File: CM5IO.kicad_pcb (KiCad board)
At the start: 4 copper layers, 160 x 90 mm, 76 parts, among them J10 690-019-298-412, J11 USB_C_Receptacle_USB2.0, J12 USB3_A, J14 JST_SHBM04B-SRSS-TB, J16 Conn_01x22_Female, J2 Conn_02x07_Odd_Even, J22 690-019-298-412, J3 Conn_01x03, J4 Bus_M.2_Socket_M, J5 Conn_01x22_Female, J6 THD-02-R, J7 Micro_SD_Card_Det, J8 THD-20-R, J9 THD-02-R, SW1 Right angle Tact button, U1 TPD4EUSB30, U12 RT9742SNGV, U18 RT9742GGJ5, U2 TPD4EUSB30, U3 MagJack-A70-112-331N126, U5 74LVC1G07SE-7, U6 AP22653W6, U7 ASEK-32.768KHZ-L-R-T, U8 AP3441SHE-7B

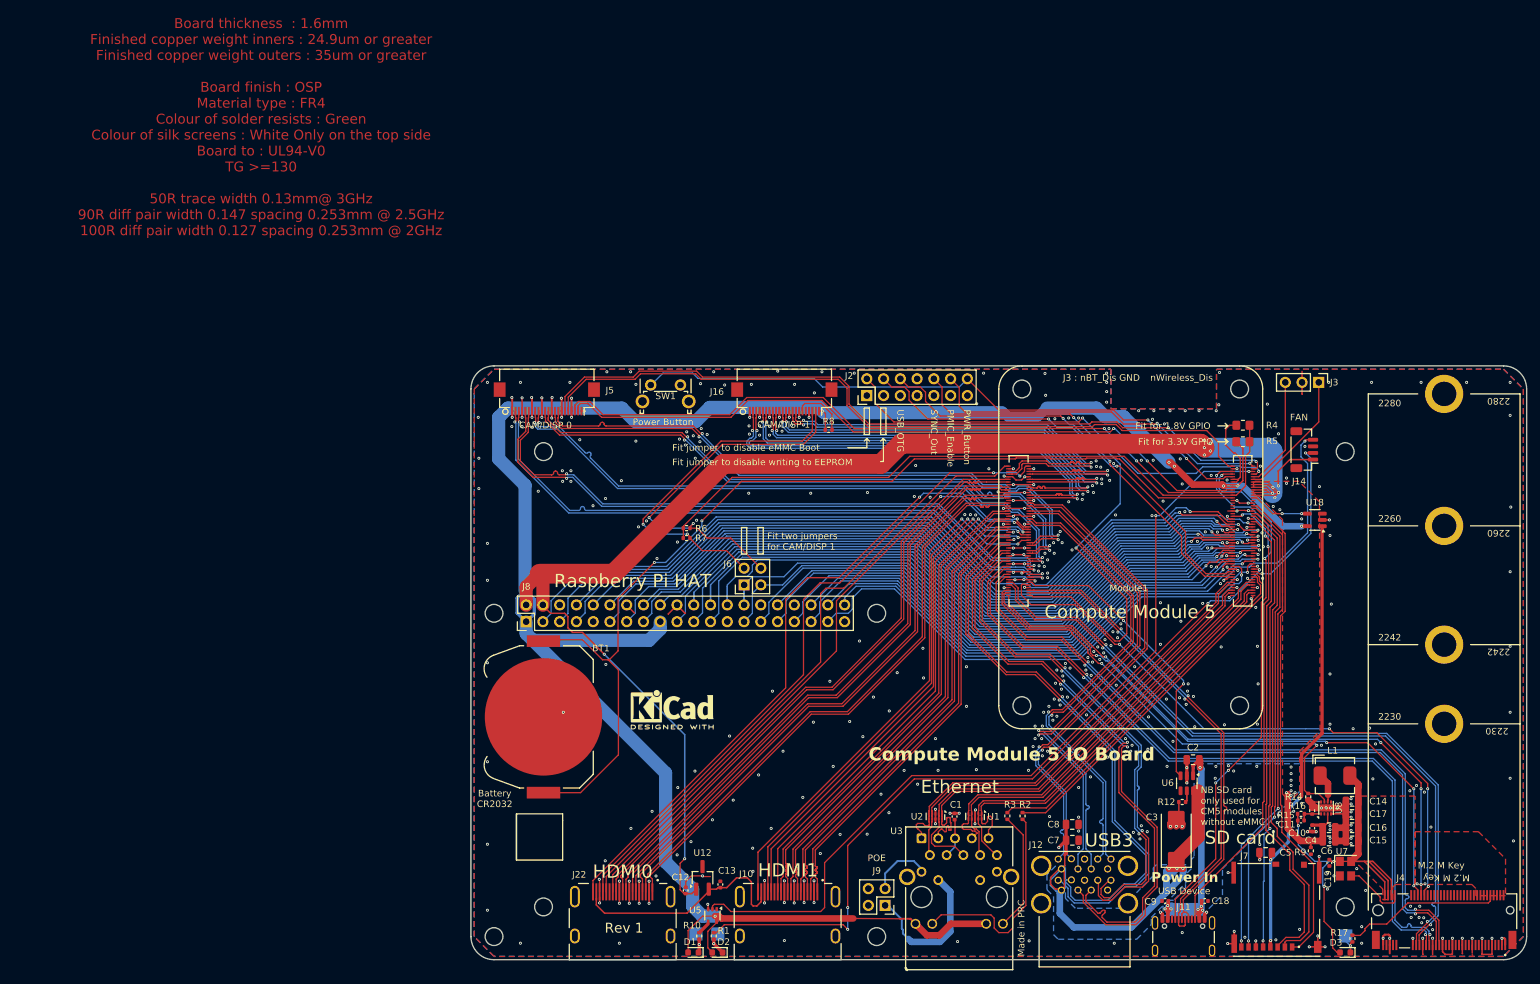
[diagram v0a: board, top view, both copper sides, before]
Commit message: remove ethernet, pcie, hdmi
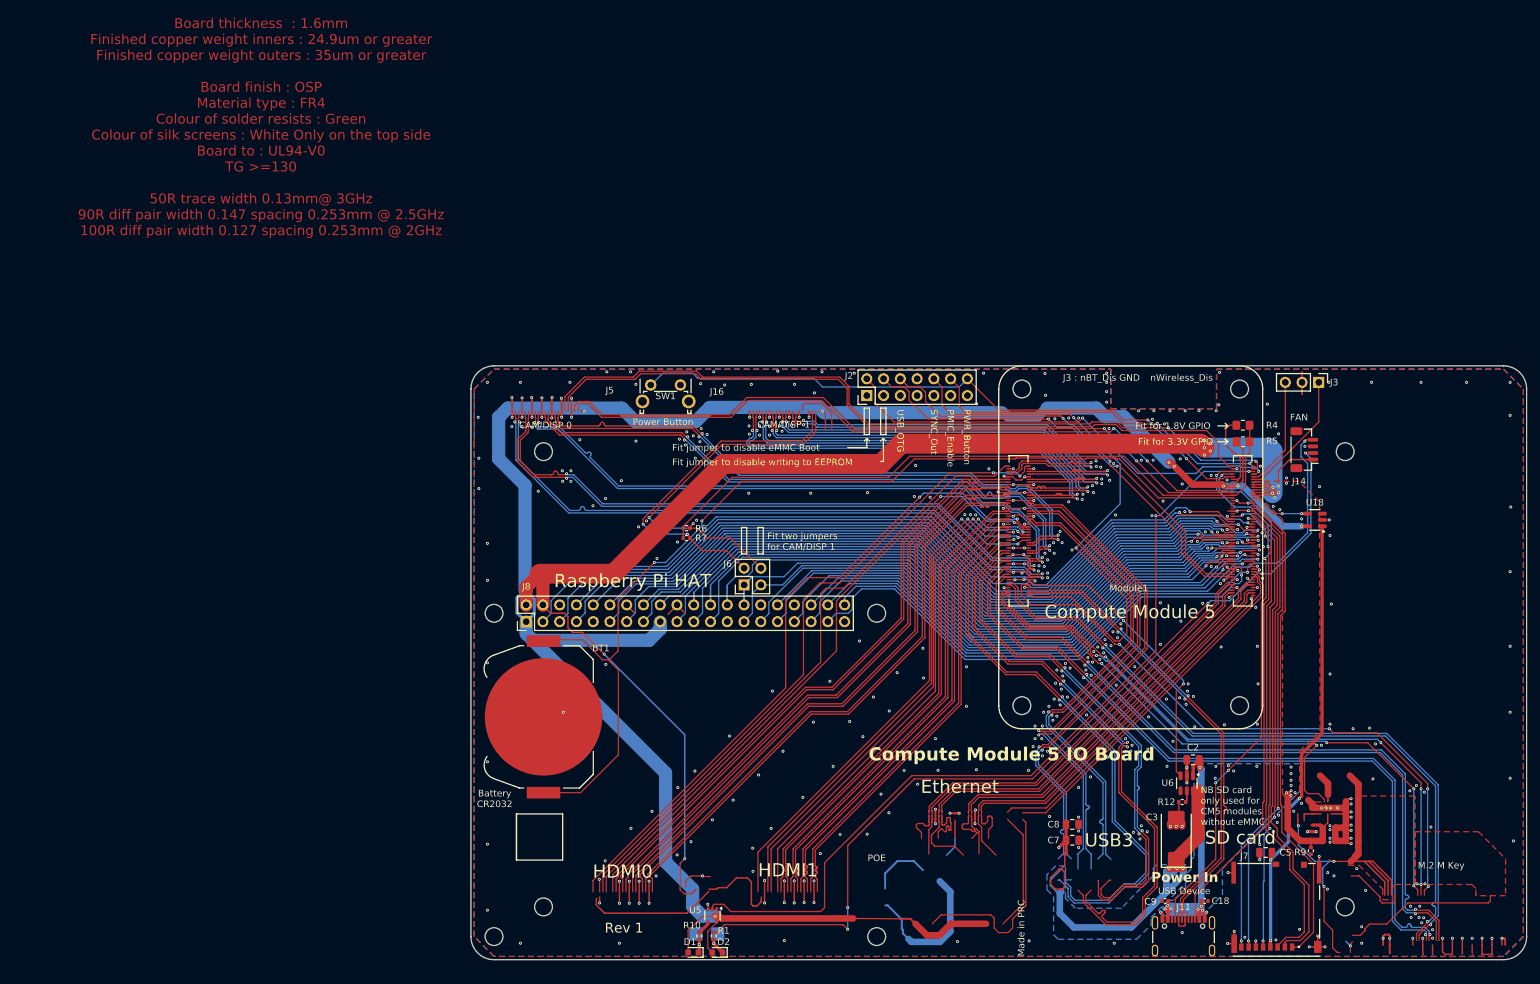
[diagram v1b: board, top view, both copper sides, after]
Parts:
- removed C1, C10, C12, C13, C19: 100n, Capacitor_SMD:C_0402_1005Metric
- removed C11: 4.7nF, Capacitor_SMD:C_0402_1005Metric
- removed C14, C15, C16, C17, C4, C6: 10u, Capacitor_SMD:C_0805_2012Metric
- removed D3: LED Green, LED_SMD:LED_0603_1608Metric
- removed J10, J22: 690-019-298-412, CM5IO:EDAC 690-019-298-412
- removed J12: USB3_A, CM5IO:MTCONN_UBAF30-D2011
- removed J16, J5: Conn_01x22_Female, CM5IO:Hirose_FH12-22S-0.5SH_1x22-1MP_P0.50mm_Horizontal
- removed J4: Bus_M.2_Socket_M, CM5IO:M.2 M Key socket
- removed J9: THD-02-R, Connector_PinHeader_2.54mm:PinHeader_2x02_P2.54mm_Vertical
- removed L1: 2.2uH, CM5IO:L_Bourns_SRP5030CC
- removed R14: 100K 1%, Resistor_SMD:R_0402_1005Metric
- removed R15: 10K 1%, Resistor_SMD:R_0402_1005Metric
- removed R16, R8: 2.2K 1%, Resistor_SMD:R_0402_1005Metric
- removed R17: 1k, Resistor_SMD:R_0402_1005Metric
- removed R2, R3: 470R, Resistor_SMD:R_0402_1005Metric
- removed TP1: TestPoint, TestPoint:TestPoint_Pad_2.0x2.0mm
- removed U1, U2: TPD4EUSB30, Package_SON:USON-10_2.5x1.0mm_P0.5mm
- removed U12: RT9742SNGV, Package_TO_SOT_SMD:TSOT-23_HandSoldering
- removed U3: MagJack-A70-112-331N126, CM5IO:TRJG0926HENL
- removed U7: ASEK-32.768KHZ-L-R-T, Crystal:Crystal_SMD_3225-4Pin_3.2x2.5mm
- removed U8: AP3441SHE-7B, Package_DFN_QFN:DFN-8-1EP_2x2mm_P0.5mm_EP1.05x1.75mm
- removed logo1: KiCad-Logo2_5mm_SilkScreen, Symbol:KiCad-Logo2_5mm_SilkScreen
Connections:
- net /CM5_GPIO ( Ethernet, GPIO, SDCARD)/+1.8v renamed /CM5_GPIO (GPIO, SDCARD)/+1.8v
- net /CM5_GPIO ( Ethernet, GPIO, SDCARD)/BT_nDis renamed /CM5_GPIO (GPIO, SDCARD)/BT_nDis
- net /CM5_GPIO ( Ethernet, GPIO, SDCARD)/EEPROM_nWP renamed /CM5_GPIO (GPIO, SDCARD)/EEPROM_nWP
- net /CM5_GPIO ( Ethernet, GPIO, SDCARD)/GPIO10 renamed /CM5_GPIO (GPIO, SDCARD)/GPIO10
- net /CM5_GPIO ( Ethernet, GPIO, SDCARD)/GPIO11 renamed /CM5_GPIO (GPIO, SDCARD)/GPIO11
- net /CM5_GPIO ( Ethernet, GPIO, SDCARD)/GPIO12 renamed /CM5_GPIO (GPIO, SDCARD)/GPIO12
- net /CM5_GPIO ( Ethernet, GPIO, SDCARD)/GPIO13 renamed /CM5_GPIO (GPIO, SDCARD)/GPIO13
- net /CM5_GPIO ( Ethernet, GPIO, SDCARD)/GPIO14 renamed /CM5_GPIO (GPIO, SDCARD)/GPIO14
- net /CM5_GPIO ( Ethernet, GPIO, SDCARD)/GPIO15 renamed /CM5_GPIO (GPIO, SDCARD)/GPIO15
- net /CM5_GPIO ( Ethernet, GPIO, SDCARD)/GPIO16 renamed /CM5_GPIO (GPIO, SDCARD)/GPIO16
- net /CM5_GPIO ( Ethernet, GPIO, SDCARD)/GPIO17 renamed /CM5_GPIO (GPIO, SDCARD)/GPIO17
- net /CM5_GPIO ( Ethernet, GPIO, SDCARD)/GPIO18 renamed /CM5_GPIO (GPIO, SDCARD)/GPIO18
- net /CM5_GPIO ( Ethernet, GPIO, SDCARD)/GPIO19 renamed /CM5_GPIO (GPIO, SDCARD)/GPIO19
- net /CM5_GPIO ( Ethernet, GPIO, SDCARD)/GPIO2 renamed /CM5_GPIO (GPIO, SDCARD)/GPIO2
- net /CM5_GPIO ( Ethernet, GPIO, SDCARD)/GPIO20 renamed /CM5_GPIO (GPIO, SDCARD)/GPIO20
- net /CM5_GPIO ( Ethernet, GPIO, SDCARD)/GPIO21 renamed /CM5_GPIO (GPIO, SDCARD)/GPIO21
- net /CM5_GPIO ( Ethernet, GPIO, SDCARD)/GPIO22 renamed /CM5_GPIO (GPIO, SDCARD)/GPIO22
- net /CM5_GPIO ( Ethernet, GPIO, SDCARD)/GPIO23 renamed /CM5_GPIO (GPIO, SDCARD)/GPIO23
- net /CM5_GPIO ( Ethernet, GPIO, SDCARD)/GPIO24 renamed /CM5_GPIO (GPIO, SDCARD)/GPIO24
- net /CM5_GPIO ( Ethernet, GPIO, SDCARD)/GPIO25 renamed /CM5_GPIO (GPIO, SDCARD)/GPIO25
- net /CM5_GPIO ( Ethernet, GPIO, SDCARD)/GPIO26 renamed /CM5_GPIO (GPIO, SDCARD)/GPIO26
- net /CM5_GPIO ( Ethernet, GPIO, SDCARD)/GPIO27 renamed /CM5_GPIO (GPIO, SDCARD)/GPIO27
- net /CM5_GPIO ( Ethernet, GPIO, SDCARD)/GPIO3 renamed /CM5_GPIO (GPIO, SDCARD)/GPIO3
- net /CM5_GPIO ( Ethernet, GPIO, SDCARD)/GPIO4 renamed /CM5_GPIO (GPIO, SDCARD)/GPIO4
- net /CM5_GPIO ( Ethernet, GPIO, SDCARD)/GPIO5 renamed /CM5_GPIO (GPIO, SDCARD)/GPIO5
- net /CM5_GPIO ( Ethernet, GPIO, SDCARD)/GPIO6 renamed /CM5_GPIO (GPIO, SDCARD)/GPIO6
- net /CM5_GPIO ( Ethernet, GPIO, SDCARD)/GPIO7 renamed /CM5_GPIO (GPIO, SDCARD)/GPIO7
- net /CM5_GPIO ( Ethernet, GPIO, SDCARD)/GPIO8 renamed /CM5_GPIO (GPIO, SDCARD)/GPIO8
- net /CM5_GPIO ( Ethernet, GPIO, SDCARD)/GPIO9 renamed /CM5_GPIO (GPIO, SDCARD)/GPIO9
- net /CM5_GPIO ( Ethernet, GPIO, SDCARD)/GPIO_VREF renamed /CM5_GPIO (GPIO, SDCARD)/GPIO_VREF
- net /CM5_GPIO ( Ethernet, GPIO, SDCARD)/ID_SC renamed /CM5_GPIO (GPIO, SDCARD)/ID_SC
- net /CM5_GPIO ( Ethernet, GPIO, SDCARD)/ID_SD renamed /CM5_GPIO (GPIO, SDCARD)/ID_SD
- net /CM5_GPIO ( Ethernet, GPIO, SDCARD)/PMIC_ENABLE renamed /CM5_GPIO (GPIO, SDCARD)/PMIC_ENABLE
- net /CM5_GPIO ( Ethernet, GPIO, SDCARD)/PWM renamed /CM5_GPIO (GPIO, SDCARD)/PWM
- net /CM5_GPIO ( Ethernet, GPIO, SDCARD)/PWR_BUT renamed /CM5_GPIO (GPIO, SDCARD)/PWR_BUT
- net /CM5_GPIO ( Ethernet, GPIO, SDCARD)/SD_CLK renamed /CM5_GPIO (GPIO, SDCARD)/SD_CLK
- net /CM5_GPIO ( Ethernet, GPIO, SDCARD)/SD_CMD renamed /CM5_GPIO (GPIO, SDCARD)/SD_CMD
- net /CM5_GPIO ( Ethernet, GPIO, SDCARD)/SD_DAT0 renamed /CM5_GPIO (GPIO, SDCARD)/SD_DAT0
- net /CM5_GPIO ( Ethernet, GPIO, SDCARD)/SD_DAT1 renamed /CM5_GPIO (GPIO, SDCARD)/SD_DAT1
- net /CM5_GPIO ( Ethernet, GPIO, SDCARD)/SD_DAT2 renamed /CM5_GPIO (GPIO, SDCARD)/SD_DAT2
- net /CM5_GPIO ( Ethernet, GPIO, SDCARD)/SD_DAT3 renamed /CM5_GPIO (GPIO, SDCARD)/SD_DAT3
- net /CM5_GPIO ( Ethernet, GPIO, SDCARD)/SD_PWR renamed /CM5_GPIO (GPIO, SDCARD)/SD_PWR
- net /CM5_GPIO ( Ethernet, GPIO, SDCARD)/SD_PWR_ON renamed /CM5_GPIO (GPIO, SDCARD)/SD_PWR_ON
- net /CM5_GPIO ( Ethernet, GPIO, SDCARD)/SYNC_OUT renamed /CM5_GPIO (GPIO, SDCARD)/SYNC_OUT
- net /CM5_GPIO ( Ethernet, GPIO, SDCARD)/TACHO renamed /CM5_GPIO (GPIO, SDCARD)/TACHO
- net /CM5_GPIO ( Ethernet, GPIO, SDCARD)/USBOTG renamed /CM5_GPIO (GPIO, SDCARD)/USBOTG
- net /CM5_GPIO ( Ethernet, GPIO, SDCARD)/VBAT renamed /CM5_GPIO (GPIO, SDCARD)/VBAT
- net /CM5_GPIO ( Ethernet, GPIO, SDCARD)/WL_nDis renamed /CM5_GPIO (GPIO, SDCARD)/WL_nDis
- net /CM5_GPIO ( Ethernet, GPIO, SDCARD)/nPWR_LED renamed /CM5_GPIO (GPIO, SDCARD)/nPWR_LED
- net /CM5_GPIO ( Ethernet, GPIO, SDCARD)/nRPIBOOT renamed /CM5_GPIO (GPIO, SDCARD)/nRPIBOOT
- C2 pad 1: /+5v -> /CM5_HighSpeed/+5v
- Module1 pad 10: /CM5_GPIO ( Ethernet, GPIO, SDCARD)/TRD0_N -> /CM5_GPIO (GPIO, SDCARD)/TRD0_N
- Module1 pad 100: /CM5_GPIO ( Ethernet, GPIO, SDCARD)/CAM_GPIO1 -> /CM5_GPIO (GPIO, SDCARD)/CAM_GPIO1
- Module1 pad 11: /CM5_GPIO ( Ethernet, GPIO, SDCARD)/TRD2_P -> /CM5_GPIO (GPIO, SDCARD)/TRD2_P
- Module1 pad 12: /CM5_GPIO ( Ethernet, GPIO, SDCARD)/TRD0_P -> /CM5_GPIO (GPIO, SDCARD)/TRD0_P
- Module1 pad 15: /CM5_GPIO ( Ethernet, GPIO, SDCARD)/ETH_LEDY -> /CM5_GPIO (GPIO, SDCARD)/ETH_LEDY
- Module1 pad 17: /CM5_GPIO ( Ethernet, GPIO, SDCARD)/ETH_LEDG -> /CM5_GPIO (GPIO, SDCARD)/ETH_LEDG
- Module1 pad 3: /CM5_GPIO ( Ethernet, GPIO, SDCARD)/TRD3_P -> /CM5_GPIO (GPIO, SDCARD)/TRD3_P
- Module1 pad 4: /CM5_GPIO ( Ethernet, GPIO, SDCARD)/TRD1_P -> /CM5_GPIO (GPIO, SDCARD)/TRD1_P
- Module1 pad 5: /CM5_GPIO ( Ethernet, GPIO, SDCARD)/TRD3_N -> /CM5_GPIO (GPIO, SDCARD)/TRD3_N
- Module1 pad 6: /CM5_GPIO ( Ethernet, GPIO, SDCARD)/TRD1_N -> /CM5_GPIO (GPIO, SDCARD)/TRD1_N
- Module1 pad 80: /CM5_HighSpeed/SCL0 -> /CM5_GPIO (GPIO, SDCARD)/SCL0
- Module1 pad 82: /CM5_HighSpeed/SDA0 -> /CM5_GPIO (GPIO, SDCARD)/SDA0
- Module1 pad 9: /CM5_GPIO ( Ethernet, GPIO, SDCARD)/TRD2_N -> /CM5_GPIO (GPIO, SDCARD)/TRD2_N
- Module1 pad 97: /CM5_GPIO ( Ethernet, GPIO, SDCARD)/CAM_GPIO0 -> /CM5_GPIO (GPIO, SDCARD)/CAM_GPIO0
- U6 pad 1: /+5v -> /CM5_HighSpeed/+5v
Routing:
- net (no net): track 0.00 -> 415.8 mm, vias 0 -> 4
- net /CM5_GPIO (GPIO, SDCARD)/CAM_GPIO0: track 0.00 -> 117.8 mm, vias 0 -> 2
- net /CM5_GPIO ( Ethernet, GPIO, SDCARD)/CAM_GPIO0: track 117.8 -> 0.00 mm, vias 2 -> 0
- net /CM5_GPIO (GPIO, SDCARD)/CAM_GPIO1: track 0.00 -> 113.1 mm
- net /CM5_GPIO ( Ethernet, GPIO, SDCARD)/CAM_GPIO1: track 113.1 -> 0.00 mm
- net /CM5_HighSpeed/SCL0: track 108.7 -> 0.00 mm, vias 2 -> 0
- net /CM5_GPIO (GPIO, SDCARD)/SCL0: track 0.00 -> 108.7 mm, vias 0 -> 2
- net /CM5_HighSpeed/SDA0: track 108.1 -> 0.00 mm, vias 2 -> 0
- net /CM5_GPIO (GPIO, SDCARD)/SDA0: track 0.00 -> 108.1 mm, vias 0 -> 2
- net /CM5_GPIO ( Ethernet, GPIO, SDCARD)/TR2_TAP: track 72.4 -> 0.00 mm
- net /CM5_GPIO ( Ethernet, GPIO, SDCARD)/TRD1_N: track 70.5 -> 0.00 mm
- net /PCIe-M2/M2_3v3: track 70.4 -> 0.00 mm, vias 3 -> 0
- net /CM5_GPIO ( Ethernet, GPIO, SDCARD)/TRD1_P: track 69.7 -> 0.00 mm
- net /CM5_GPIO ( Ethernet, GPIO, SDCARD)/TRD0_P: track 68.2 -> 0.00 mm
- net /CM5_GPIO ( Ethernet, GPIO, SDCARD)/TRD0_N: track 67.5 -> 0.00 mm
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- added copper zone on F.Cu, net (none)
- removed copper zone on F.Cu, net /PCIe-M2/M2_3v3
